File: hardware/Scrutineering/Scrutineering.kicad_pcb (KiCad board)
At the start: 2 copper layers, 48.9 x 51.6 mm, 22 parts, among them J1 Conn_02x04, J10 Conn_01x01, J11 Conn_01x02, J12 Conn_01x02, J2 Conn_02x04, J3 Conn_01x03, J4 Conn_01x03, J5 Conn_01x01, J6 Conn_01x01, J7 Conn_01x01, J8 Conn_01x01, J9 Conn_01x01

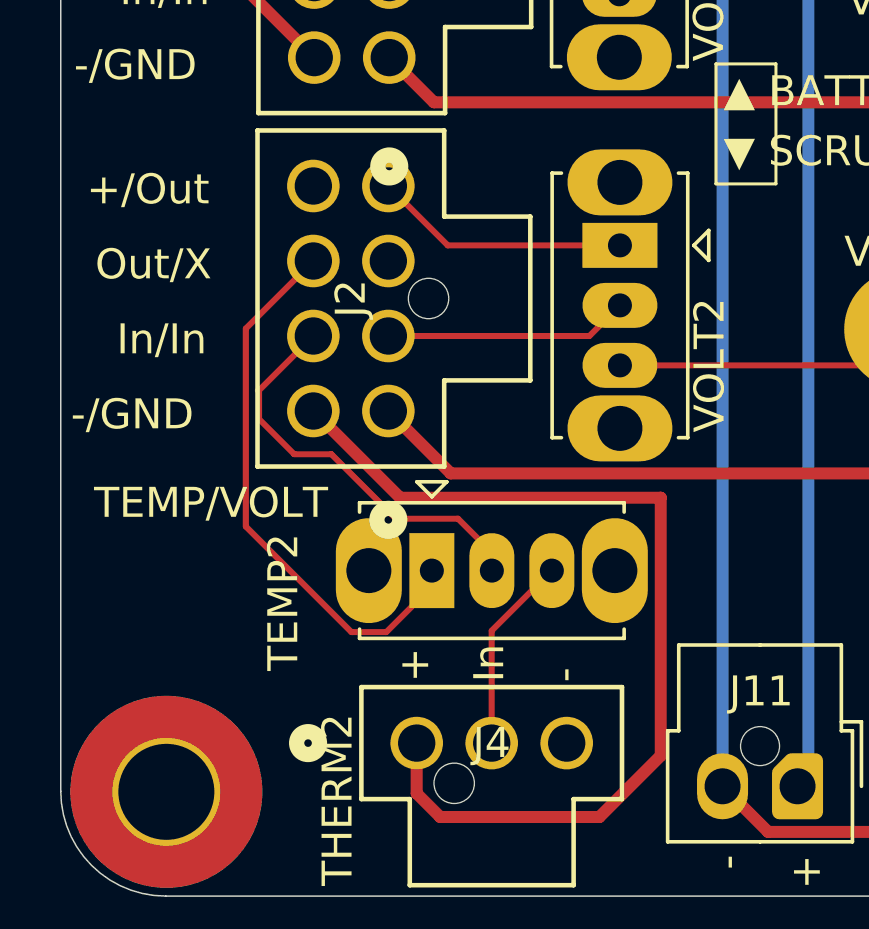
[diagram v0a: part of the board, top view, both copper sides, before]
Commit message: fix 1 trace
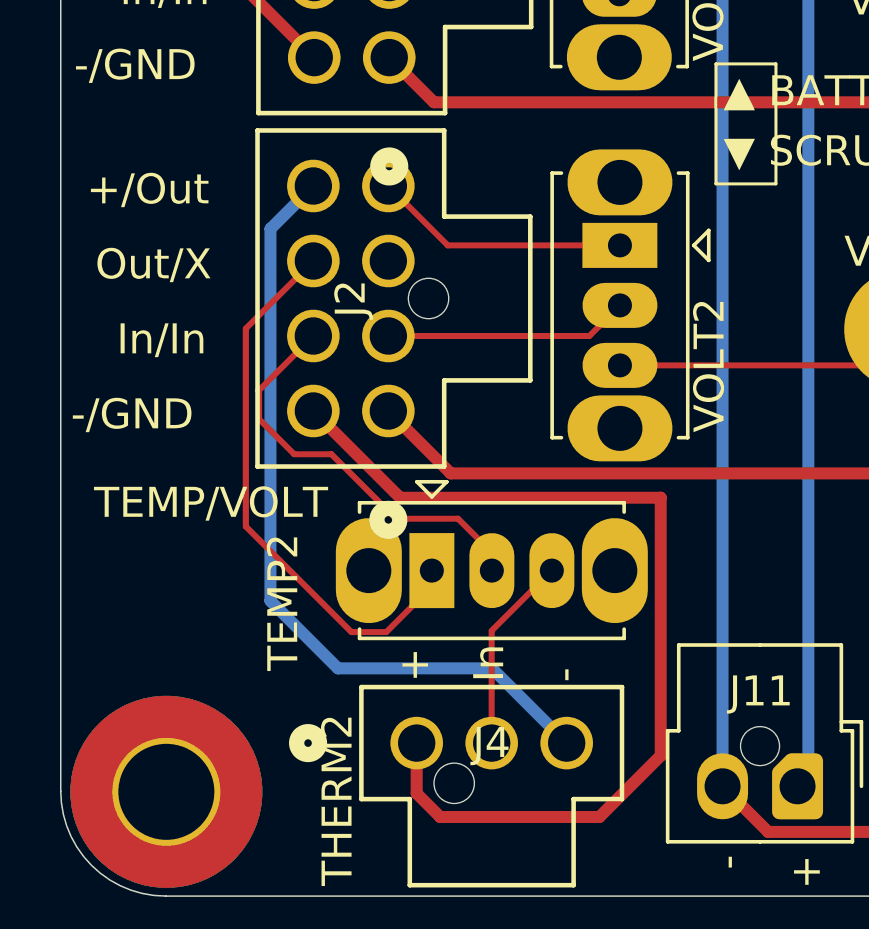
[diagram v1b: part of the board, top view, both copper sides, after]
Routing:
- net /VDDA_8: track 0.00 -> 26.3 mm
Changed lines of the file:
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@@
+	)
+	(segment
+		(start 98.25 94.25)
+		(end 98.25 81.85)
+		(width 0.4)
+		(layer "B.Cu")
+		(net 14)
+	)
+	(segment
+		(start 100.5 96.5)
+		(end 98.25 94.25)
+		(width 0.4)
+		(layer "B.Cu")
+		(net 14)
+	)
+	(segment
+		(start 105.63505 96.5)
+		(end 100.5 96.5)
+		(width 0.4)
+		(layer "B.Cu")
+		(net 14)
+	)
+	(segment
+		(start 98.25 81.85)
+		(end 99.68 80.42)
+		(width 0.4)
+		(layer "B.Cu")
+		(net 14)
+	)
+	(segment
+		(start 108.1249 98.98985)
+		(end 105.63505 96.5)
+		(width 0.4)
+		(layer "B.Cu")
+		(net 14)
 	)
 	(segment

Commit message: Revert "fix 1 trace"
This reverts commit af0c854c5f9be3b18890f8714f235c97d2fe5d90.

:#
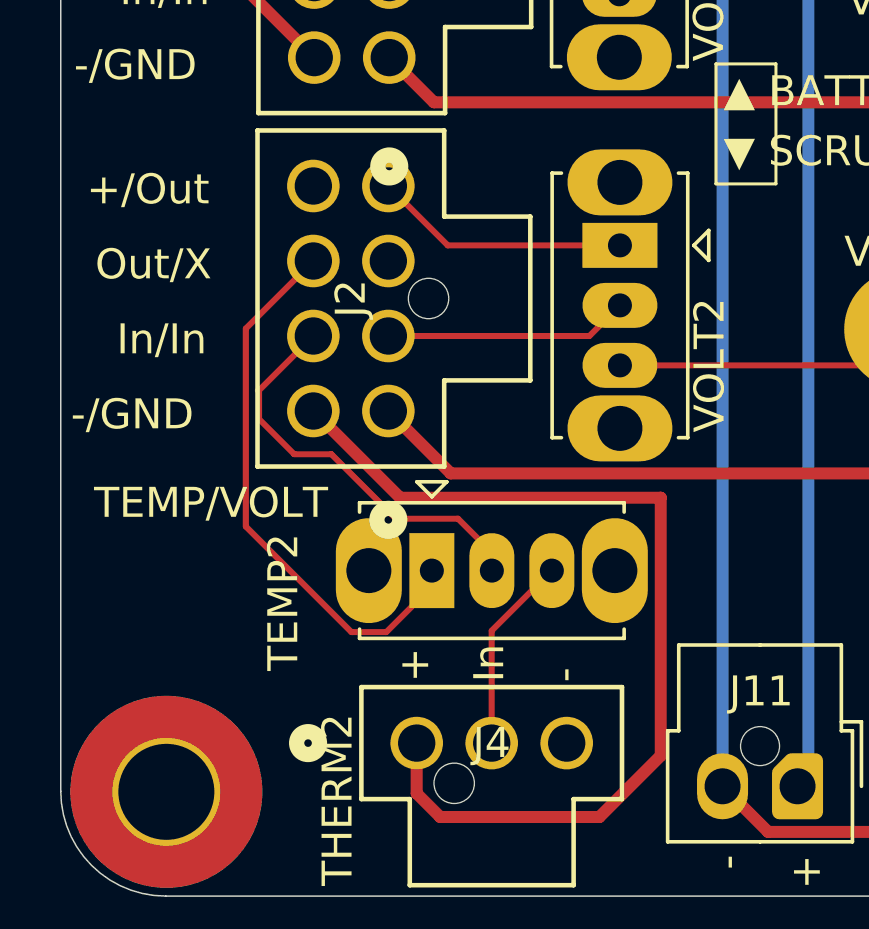
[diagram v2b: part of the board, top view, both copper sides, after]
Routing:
- net /VDDA_8: track 26.3 -> 0.00 mm
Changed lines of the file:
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@@
-	)
-	(segment
-		(start 98.25 94.25)
-		(end 98.25 81.85)
-		(width 0.4)
-		(layer "B.Cu")
-		(net 14)
-	)
-	(segment
-		(start 100.5 96.5)
-		(end 98.25 94.25)
-		(width 0.4)
-		(layer "B.Cu")
-		(net 14)
-	)
-	(segment
-		(start 105.63505 96.5)
-		(end 100.5 96.5)
-		(width 0.4)
-		(layer "B.Cu")
-		(net 14)
-	)
-	(segment
-		(start 98.25 81.85)
-		(end 99.68 80.42)
-		(width 0.4)
-		(layer "B.Cu")
-		(net 14)
-	)
-	(segment
-		(start 108.1249 98.98985)
-		(end 105.63505 96.5)
-		(width 0.4)
-		(layer "B.Cu")
-		(net 14)
 	)
 	(segment
